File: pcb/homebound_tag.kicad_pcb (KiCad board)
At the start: 2 copper layers, 22.4 x 22.4 mm, 2 parts, among them U1 NTAG216

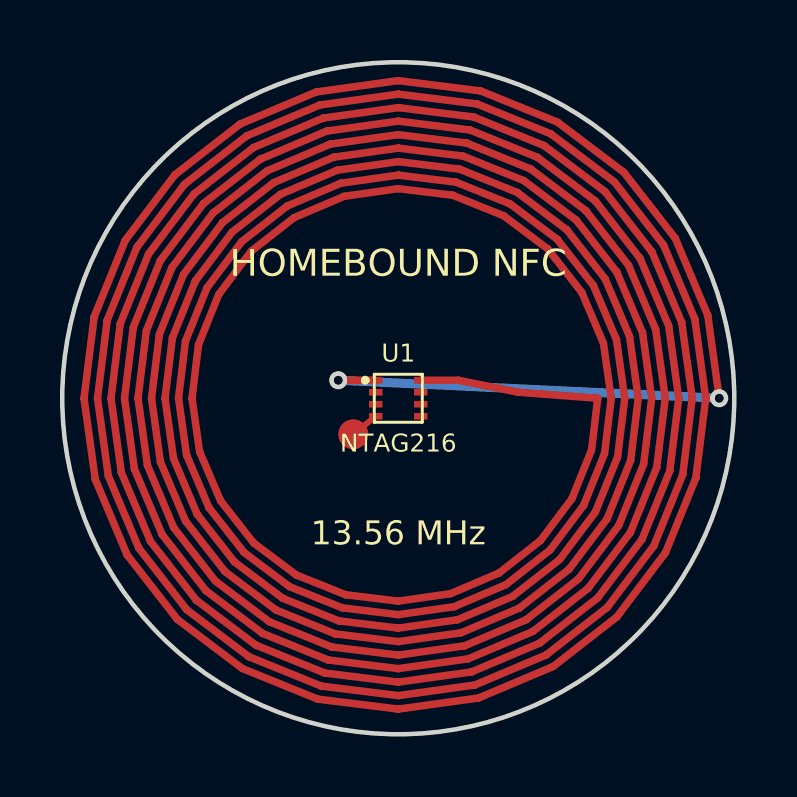
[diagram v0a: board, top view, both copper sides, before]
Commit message: Fix PCB copper-to-edge clearance, add check.py geometry DRC, and update docs
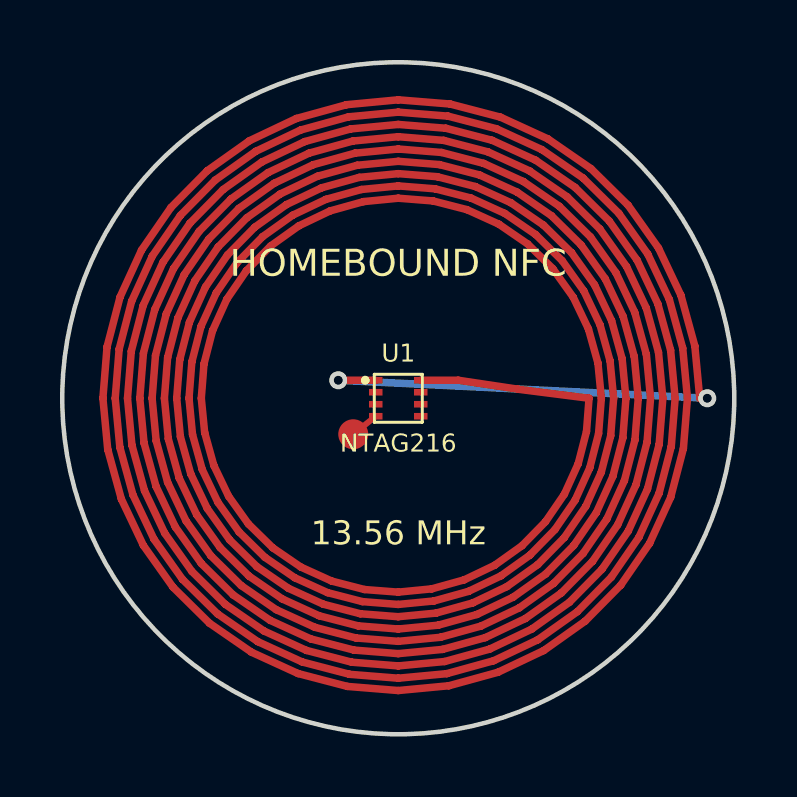
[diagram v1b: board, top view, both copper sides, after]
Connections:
- U1 pad 1: ANT_A -> ANT
- U1 pad 8: ANT_B -> ANT
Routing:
- net ANT_A: track 503.1 -> 0.00 mm, vias 2 -> 0
- net ANT: track 0.00 -> 482.9 mm, vias 0 -> 2
- net ANT_B: track 5.95 -> 0.00 mm
